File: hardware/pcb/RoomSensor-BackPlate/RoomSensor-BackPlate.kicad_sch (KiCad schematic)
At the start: 12 parts, among them SW1 Voltage EX1, SW2 Voltage EX2, U1 PCF8574P

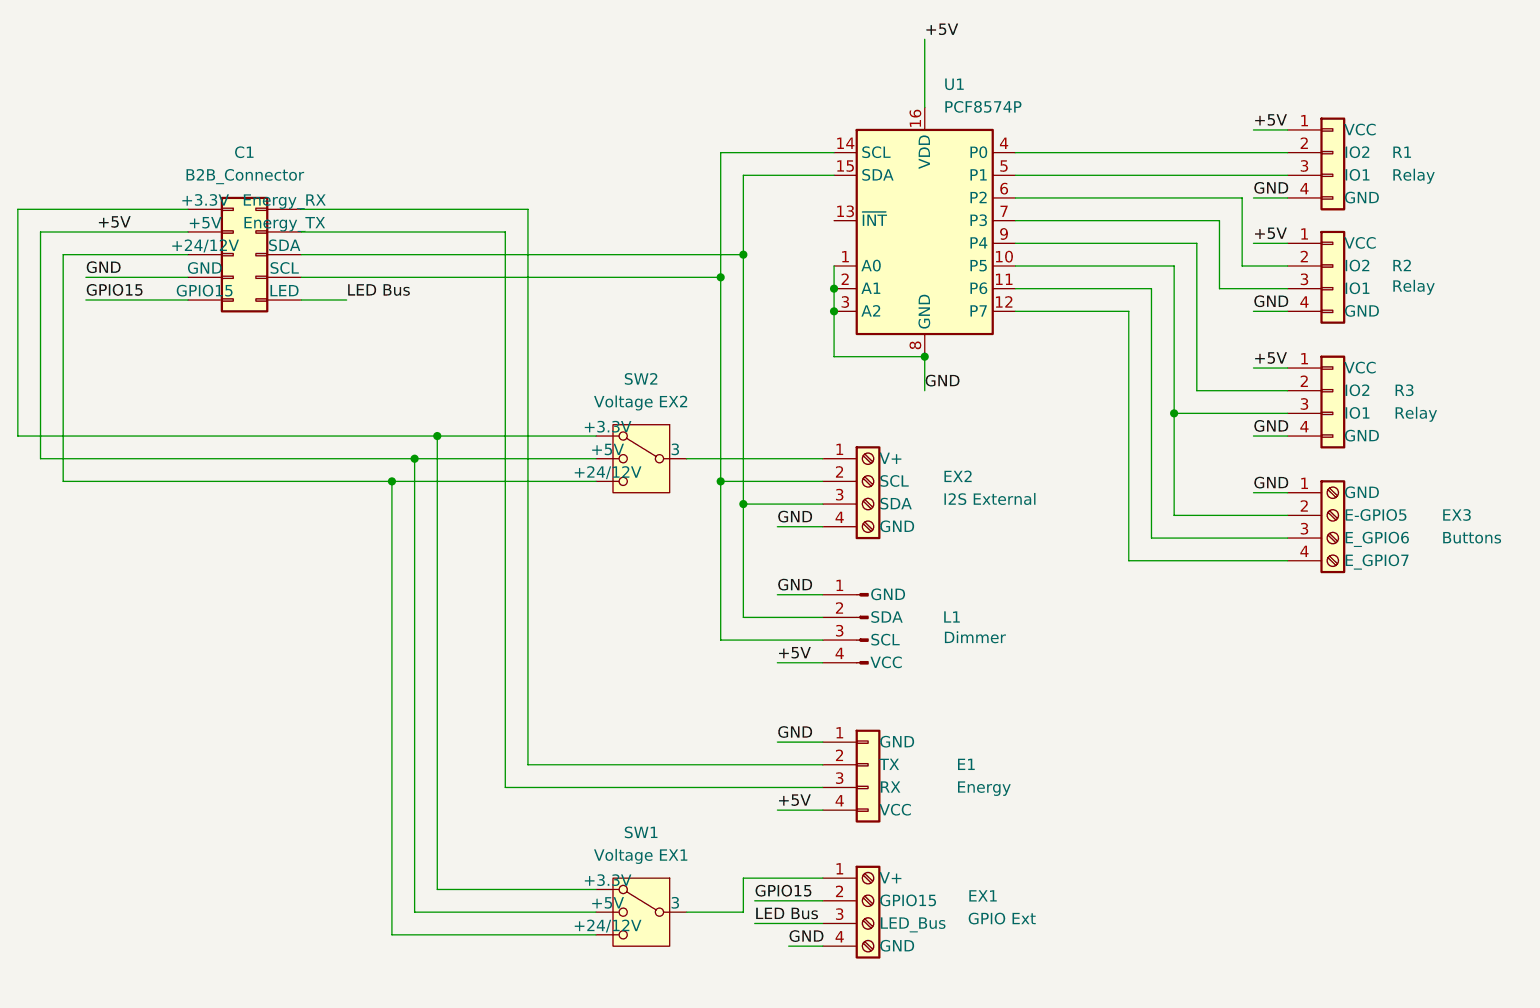
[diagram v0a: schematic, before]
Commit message: hardware: move footprint/symbol libs into pcb/, update KiCad project settings
Move room-sensor.pretty/ and room-sensor.kicad_sym into hardware/pcb/ so all
PCB design files live under one directory. Also picks up KiCad project edits:
BOM preset config and pin_to_pin ERC rule change to error on both plates.

Co-Authored-By: Claude Sonnet 4.6 <noreply@anthropic.com>
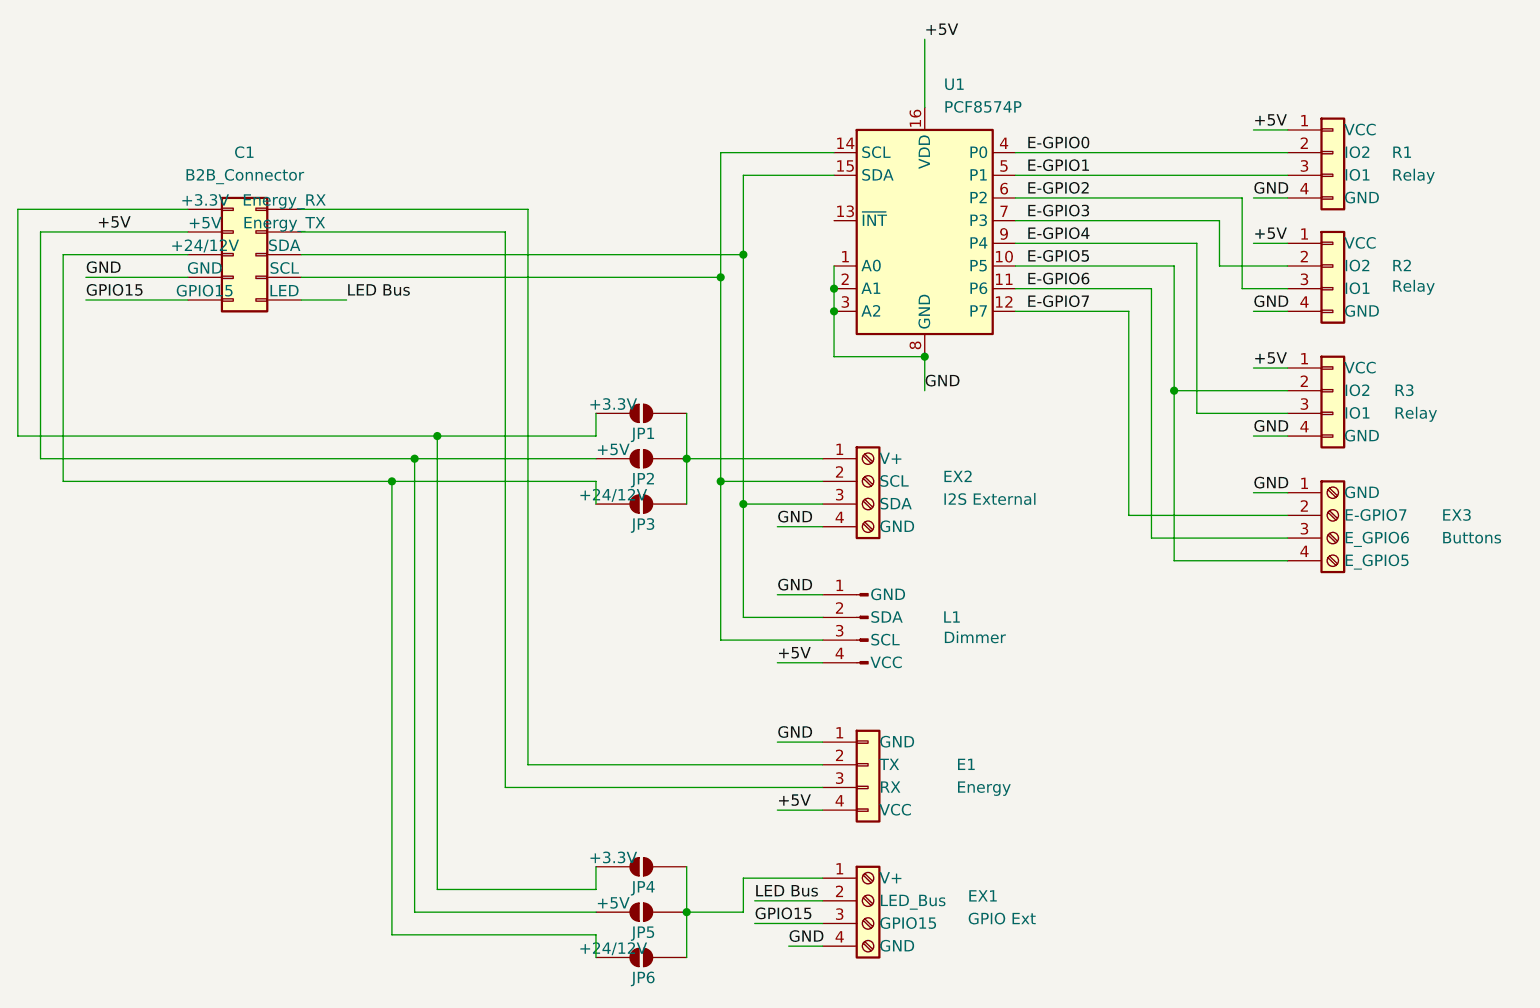
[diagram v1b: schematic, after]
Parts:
- removed SW1: Voltage EX1, Button_Switch_THT:SW_DIP_SPSTx02_Slide_9.78x7.26mm_W7.62mm_P2.54mm, symbol Switch:SW_SP3T
- removed SW2: Voltage EX2, Button_Switch_THT:SW_DIP_SPSTx02_Slide_9.78x7.26mm_W7.62mm_P2.54mm, symbol Switch:SW_SP3T
- added JP1, JP2, JP3, JP4, JP5, JP6: SolderJumper_2_Open, Jumper:SolderJumper-2_P1.3mm_Open_Pad1.0x1.5mm, symbol Jumper:SolderJumper_2_Open
- C1: MPN (none) -> MTB10-10S
- E1, L1, R1, R2, R3: MPN (none) -> HX PM2.54-1x4P ZC H11
- EX1, EX2, EX3: footprint TerminalBlock:TerminalBlock_Xinya_XY308-2.54-4P_1x04_P2.54mm_Horizontal -> TerminalBlock_Phoenix:TerminalBlock_Phoenix_MPT-0,5-4-2.54_1x04_P2.54mm_Horizontal; MPN (none) -> KF128-2.54-4P
- U1: MPN (none) -> PCF8574P
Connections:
- net +5V: now also JP2.1 (+5V), JP5.1 (+5V)
- net GPIO15: now also EX1.3 (GPIO15); no longer EX1.2 (GPIO15)
- net LED Bus: now also EX1.2 (LED_Bus); no longer EX1.3 (LED_Bus)
- net at C1.1 (+3.3V): now also JP1.1 (+3.3V), JP4.1 (+3.3V)
- net at C1.5 (+24/12V): now also JP3.1 (+24/12V), JP6.1 (+24/12V)
- net E-GPIO4: now reaches U1.9 (P4)
- net E-GPIO4: now also R3.3 (IO1); no longer R3.2 (IO2)
- net at EX1.1 (V+): now also JP4.2, JP5.2, JP6.2
- net at EX2.1 (V+): now also JP1.2, JP2.2, JP3.2
- net E-GPIO2: now reaches U1.6 (P2)
- net E-GPIO2: now also R2.3 (IO1); no longer R2.2 (IO2)
- net E-GPIO3: now reaches U1.7 (P3)
- net E-GPIO3: now also R2.2 (IO2); no longer R2.3 (IO1)
- net E-GPIO0: now reaches R1.2 (IO2), U1.4 (P0)
- net E-GPIO1: now reaches R1.3 (IO1), U1.5 (P1)
- net E-GPIO6: now reaches EX3.3 (E_GPIO6), U1.11 (P6)
- net E-GPIO5: now reaches EX3.4 (E_GPIO5)
- net E-GPIO5: now also R3.2 (IO2), U1.10 (P5); no longer U1.12 (P7)
- new net E-GPIO7: EX3.2 (E-GPIO7), U1.12 (P7)

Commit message: hardware: back plate mounting holes + EX2 routing, plot settings cleanup
BackPlate: add four M3 mounting holes, re-place EX2 (I2S External) and
route the remaining nets (+26 track segments, 7 new schematic wires).
MainPlate: switch plot output to a repo-relative directory instead of a
local Desktop path, add board outline/keepout drawings.

Co-Authored-By: Claude Opus 5 (1M context) <noreply@anthropic.com>
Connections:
- net E-GPIO0: now also R3.2 (IO2); no longer R1.2 (IO2)
- net E-GPIO1: now also R3.3 (IO1); no longer R1.3 (IO1)
- net E-GPIO2: now also R2.2 (IO2); no longer R2.3 (IO1)
- net E-GPIO3: now also R2.3 (IO1); no longer R2.2 (IO2)
- net E-GPIO4: now also R1.2 (IO2); no longer R3.3 (IO1)
- net E-GPIO5: now also R1.3 (IO1); no longer R3.2 (IO2)
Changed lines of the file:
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@@
-	)
-	(junction
-		(at 154.94 64.77)
-		(diameter 0)
-		(color 0 0 0 0)
 	)
 	(junction
@@
 	)
 	(junction
+		(at 154.94 50.8)
+		(diameter 0)
+		(color 0 0 0 0)
+	)
+	(junction
 		(at 100.33 123.19)
 		(diameter 0)
@@
 	(wire
 		(pts
-			(xy 137.16 38.1) (xy 167.64 38.1)
-		)
-		(stroke
-			(width 0)
-			(type default)
-		)
-	)
-	(wire
-		(pts
 			(xy 67.31 125.73) (xy 67.31 74.93)
 		)
@@
 	(wire
 		(pts
+			(xy 162.56 43.18) (xy 162.56 50.8)
+		)
+		(stroke
+			(width 0)
+			(type default)
+		)
+	)
+	(wire
+		(pts
 			(xy 149.86 55.88) (xy 149.86 78.74)
 		)
@@
 	(wire
 		(pts
+			(xy 154.94 36.83) (xy 161.29 36.83)
+		)
+		(stroke
+			(width 0)
+			(type default)
+		)
+	)
+	(wire
+		(pts
 			(xy 90.17 67.31) (xy 90.17 69.85)
 		)
@@
 	(wire
 		(pts
+			(xy 161.29 50.8) (xy 154.94 50.8)
+		)
+		(stroke
+			(width 0)
+			(type default)
+		)
+	)
+	(wire
+		(pts
 			(xy 106.68 40.64) (xy 106.68 49.53)
 		)
@@
 	(wire
 		(pts
-			(xy 167.64 40.64) (xy 137.16 40.64)
+			(xy 154.94 48.26) (xy 154.94 36.83)
+		)
+		(stroke
+			(width 0)
+			(type default)
+		)
+	)
+	(wire
+		(pts
+			(xy 161.29 40.64) (xy 167.64 40.64)
+		)
+		(stroke
+			(width 0)
+			(type default)
+		)
+	)
+	(wire
+		(pts
+			(xy 167.64 64.77) (xy 158.75 64.77)
+		)
+		(stroke
+			(width 0)
+			(type default)
+		)
+	)
+	(wire
+		(pts
+			(xy 162.56 50.8) (xy 167.64 50.8)
 		)
 		(stroke
@@
 	(wire
 		(pts
-			(xy 162.56 53.34) (xy 167.64 53.34)
-		)
-		(stroke
-			(width 0)
-			(type default)
-		)
-	)
-	(wire
-		(pts
 			(xy 100.33 123.19) (xy 100.33 128.27)
 		)
@@
 	(wire
 		(pts
+			(xy 156.21 67.31) (xy 156.21 40.64)
+		)
+		(stroke
+			(width 0)
+			(type default)
+		)
+	)
+	(wire
+		(pts
 			(xy 104.14 52.07) (xy 104.14 74.93)
 		)
@@
 	(wire
 		(pts
-			(xy 162.56 43.18) (xy 162.56 53.34)
+			(xy 160.02 53.34) (xy 167.64 53.34)
 		)
 		(stroke
@@
 	(wire
 		(pts
-			(xy 154.94 64.77) (xy 167.64 64.77)
-		)
-		(stroke
-			(width 0)
-			(type default)
-		)
-	)
-	(wire
-		(pts
 			(xy 80.01 109.22) (xy 115.57 109.22)
 		)
@@
 	(wire
 		(pts
-			(xy 157.48 67.31) (xy 167.64 67.31)
-		)
-		(stroke
-			(width 0)
-			(type default)
-		)
-	)
-	(wire
-		(pts
 			(xy 163.83 43.18) (xy 167.64 43.18)
 		)
@@
 	(wire
 		(pts
-			(xy 160.02 50.8) (xy 167.64 50.8)
-		)
-		(stroke
-			(width 0)
-			(type default)
-		)
-	)
-	(wire
-		(pts
 			(xy 90.17 69.85) (xy 72.39 69.85)
 		)
@@
 	(wire
 		(pts
-			(xy 157.48 48.26) (xy 157.48 67.31)
-		)
-		(stroke
-			(width 0)
-			(type default)
-		)
-	)
-	(wire
-		(pts
 			(xy 72.39 120.65) (xy 72.39 69.85)
 		)
@@
 	(wire
 		(pts
-			(xy 137.16 48.26) (xy 157.48 48.26)
-		)
-		(stroke
-			(width 0)
-			(type default)
-		)
-	)
-	(wire
-		(pts
 			(xy 104.14 74.93) (xy 104.14 92.71)
 		)
@@
 	(wire
 		(pts
-			(xy 154.94 64.77) (xy 154.94 83.82)
-		)
-		(stroke
-			(width 0)
-			(type default)
-		)
-	)
-	(wire
-		(pts
 			(xy 149.86 78.74) (xy 167.64 78.74)
 		)
@@
 	(wire
 		(pts
-			(xy 154.94 50.8) (xy 154.94 64.77)
+			(xy 154.94 50.8) (xy 154.94 83.82)
 		)
 		(stroke
@@
 	(wire
 		(pts
+			(xy 158.75 64.77) (xy 158.75 38.1)
+		)
+		(stroke
+			(width 0)
+			(type default)
+		)
+	)
+	(wire
+		(pts
+			(xy 161.29 36.83) (xy 161.29 38.1)
+		)
+		(stroke
+			(width 0)
+			(type default)
+		)
+	)
+	(wire
+		(pts
 			(xy 90.17 123.19) (xy 69.85 123.19)
 		)
@@
 	(wire
 		(pts
-			(xy 160.02 45.72) (xy 160.02 50.8)
+			(xy 160.02 45.72) (xy 160.02 53.34)
+		)
+		(stroke
+			(width 0)
+			(type default)
+		)
+	)
+	(wire
+		(pts
+			(xy 158.75 38.1) (xy 137.16 38.1)
 		)
 		(stroke
@@
 	(wire
 		(pts
+			(xy 167.64 67.31) (xy 156.21 67.31)
+		)
+		(stroke
+			(width 0)
+			(type default)
+		)
+	)
+	(wire
+		(pts
+			(xy 161.29 40.64) (xy 161.29 50.8)
+		)
+		(stroke
+			(width 0)
+			(type default)
+		)
+	)
+	(wire
+		(pts
 			(xy 82.55 106.68) (xy 115.57 106.68)
 		)
@@
 	(wire
 		(pts
+			(xy 156.21 40.64) (xy 137.16 40.64)
+		)
+		(stroke
+			(width 0)
+			(type default)
+		)
+	)
+	(wire
+		(pts
+			(xy 137.16 48.26) (xy 154.94 48.26)
+		)
+		(stroke
+			(width 0)
+			(type default)
+		)
+	)
+	(wire
+		(pts
 			(xy 116.84 60.96) (xy 127 60.96)
 		)
@@
 		)
 		(stroke
+			(width 0)
+			(type default)
+		)
+	)
+	(wire
+		(pts
+			(xy 161.29 38.1) (xy 167.64 38.1)
+		)
+		(stroke
